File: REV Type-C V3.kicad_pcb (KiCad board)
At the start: 2 copper layers, 47 x 21.6 mm, 34 parts, among them J1 USB_B_Mini, J2 USB_A, J3 USB_C_Receptacle_USB2.0, U1 USB2422, U2 MIC5504-3.3YM5, Y1 24M

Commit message: V3 Preliminary Files
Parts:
- moved REF** 1.27 mm to (154.9, 85.1)
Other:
- board size 47 x 21.6 mm -> 45.7 x 21.6 mm
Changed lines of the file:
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@@
       (outputformat 1)
       (mirror false)
-      (drillshape 1)
+      (drillshape 0)
       (scaleselection 1)
       (outputdirectory ""))
@@
   )
   (module MountingHole:MountingHole_3.2mm_M3 (layer F.Cu)
-    (at 156.21 85.09)
+    (at 154.94 85.09)
     (descr "Mounting Hole 3.2mm, no annular, M3")
     (tags "mounting hole 3.2mm no annular m3")
@@
     )
   )
-  (gr_text "copr.cc//XXXX\n" (at 147.32 85.09) (layer F.SilkS)
+  (gr_text "copr.cc//XXXX\n" (at 146.05 86.36) (layer F.SilkS)
     (effects (font (size 1 1) (thickness 0.15)))
   )
   (gr_line (start 111.76 72.39) (end 111.76 66.04) (layer Edge.Cuts) (width 0.05))
-  (gr_line (start 158.75 66.04) (end 111.76 66.04) (layer Edge.Cuts) (width 0.05))
-  (gr_line (start 158.75 66.04) (end 158.75 87.63) (layer Edge.Cuts) (width 0.05))
+  (gr_line (start 157.48 66.04) (end 111.76 66.04) (layer Edge.Cuts) (width 0.05))
+  (gr_line (start 157.48 66.04) (end 157.48 87.63) (layer Edge.Cuts) (width 0.05))
   (gr_line (start 111.76 87.63) (end 111.76 72.39) (layer Edge.Cuts) (width 0.05))
-  (gr_line (start 158.75 87.63) (end 111.76 87.63) (layer Edge.Cuts) (width 0.05))
+  (gr_line (start 157.48 87.63) (end 111.76 87.63) (layer Edge.Cuts) (width 0.05))
   (gr_text "3V3\n\n" (at 135.39 78.74) (layer F.SilkS)
     (effects (font (size 1.5 1.5) (thickness 0.3)))
@@
     (polygon
       (pts
-        (xy 158.75 66.04) (xy 111.76 66.04) (xy 111.76 87.63) (xy 158.75 87.63)
+        (xy 157.48 66.04) (xy 111.76 66.04) (xy 111.76 87.63) (xy 157.48 87.63)
       )
     )

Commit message: Fixed wrong Mini-B connector footprint
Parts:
- J1: footprint Connector_USB:USB_Mini-B_Tensility_54-00023_Vertical -> Connector_USB:UX20-MB-5P
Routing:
- net +5V: track 70.4 -> 75.2 mm
- net /D1+: track 29.5 -> 27.6 mm
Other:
- board text added: "ExH Type-C v3"

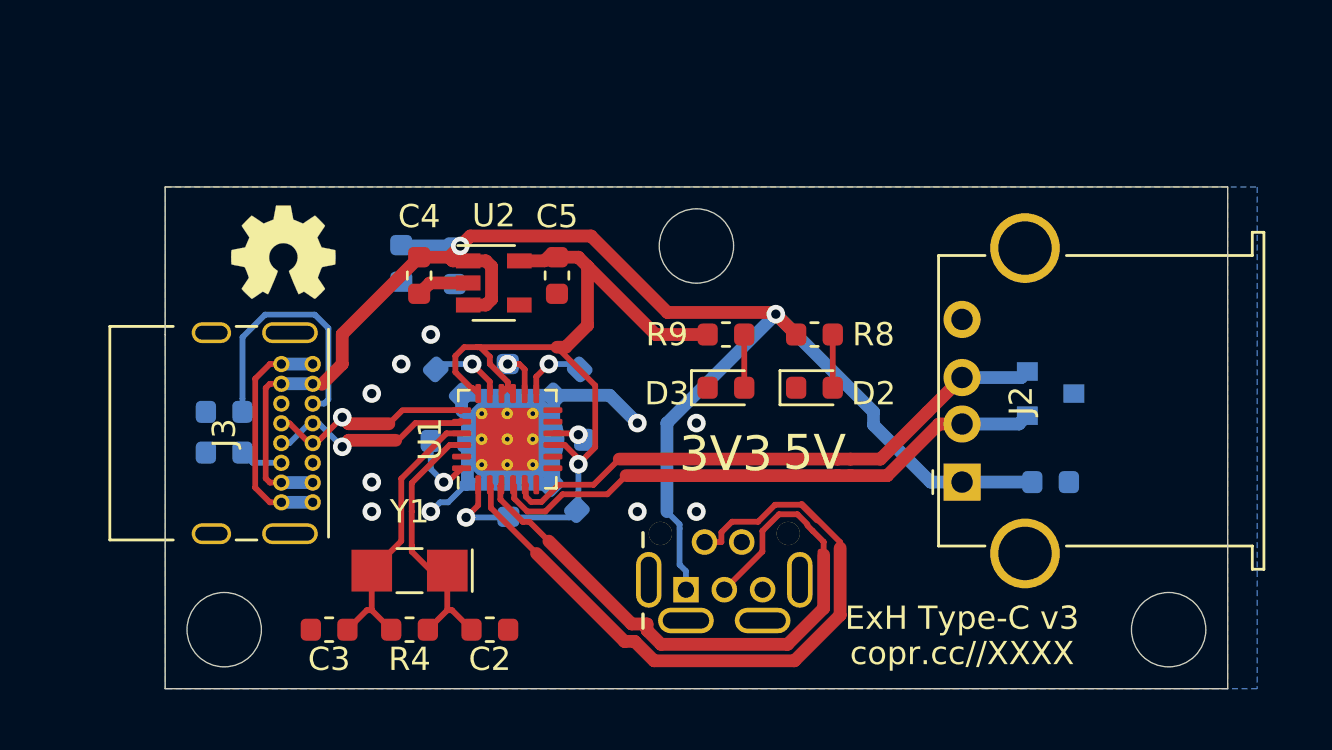
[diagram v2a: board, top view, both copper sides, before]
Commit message: Add Copperforge P/N; potential one-sided V3 layout
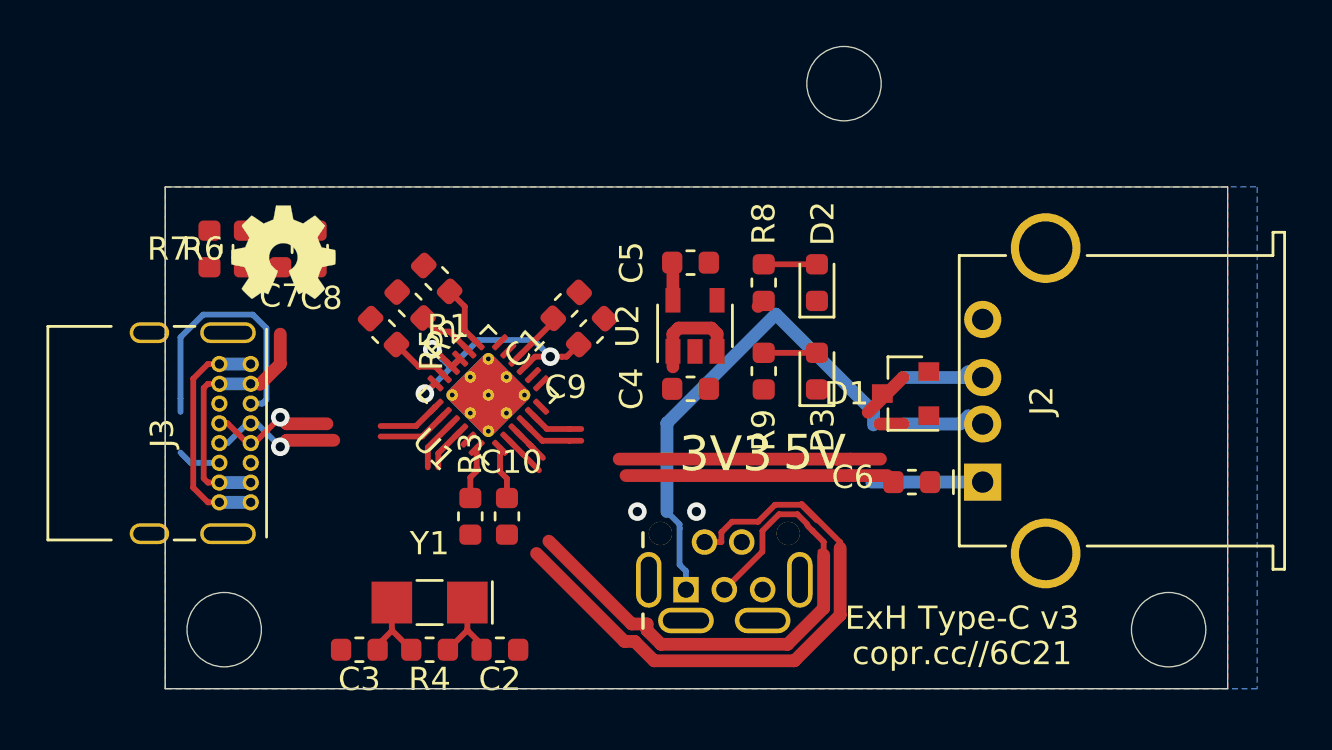
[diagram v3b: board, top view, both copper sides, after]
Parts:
- C1, C10, C6, C7, C8, C9, D1, R1, R2, R3, R5, R6, R7: moved to F.Cu
- moved LOGO 16.0 mm to (130.7, 85.1)
- moved C4 12.7 mm to (134.4, 74.7), turned to 0 degrees
- moved REF** 9.44 mm to (141.0, 61.6)
- moved U2 8.85 mm to (134.6, 72.0), turned to 90 degrees
- moved R7 8.79 mm to (113.7, 68.7), turned to 90 degrees
- moved C9 7.23 mm to (130.1, 72.3), turned to 45 degrees
- moved R1 7.16 mm to (123.4, 70.0), turned to 135 degrees
- moved R6 7.07 mm to (115.2, 68.7), turned to 270 degrees
- moved D1 6.24 mm to (143.6, 74.9), turned to 180 degrees
- moved C8 6.03 mm to (118.2, 68.7), turned to 90 degrees
- moved C6 5.97 mm to (143.9, 78.7), turned to 180 degrees
- moved C1 5.79 mm to (129.0, 71.1), turned to 225 degrees
- moved C5 5.77 mm to (134.4, 69.3), turned to 0 degrees
- moved R2 5.36 mm to (122.3, 71.1), turned to 135 degrees
- moved C7 5.24 mm to (116.7, 68.7), turned to 90 degrees
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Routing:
- net +5V: track 75.2 -> 40.3 mm, vias 2 -> 0
- net +3V3: track 39.6 -> 17.1 mm, vias 2 -> 3
- net /D2+: track 24.6 -> 5.25 mm
- net /D2-: track 24.7 -> 6.70 mm
- net /XTAL_O: track 12.2 -> 5.82 mm
- net /XTAL_I: track 11.2 -> 5.43 mm
- net /D1-: track 31.1 -> 29.2 mm
- net /D1+: track 27.6 -> 26.0 mm
- net Net-(C1-Pad2): track 1.12 -> 2.41 mm, vias 1 -> 0
- net Net-(R3-Pad1): track 3.02 -> 2.27 mm, vias 1 -> 0
- net Net-(R5-Pad2): track 3.25 -> 2.58 mm, vias 1 -> 0
- net /DIN-: track 8.93 -> 8.26 mm
- net Net-(R2-Pad1): track 2.00 -> 2.53 mm, vias 1 -> 0
- net GND: track 34.5 -> 34.8 mm, vias 10 -> 2
- net Net-(R1-Pad1): track 2.92 -> 2.67 mm, vias 1 -> 0
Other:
- board text added: "Designed by DoubleDIP in collaboration with"
- board text added: "USB Type-C Adapter for REV Expansion Hub"
- board text added: "copr.cc//6C21"
- board text removed: "copr.cc//XXXX"
